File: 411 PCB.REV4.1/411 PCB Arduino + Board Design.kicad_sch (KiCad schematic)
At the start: 37 parts, among them J1 ICSP CONN, J3 Conn_01x04, J4 Conn_01x05_Pin, Q1 Q_NMOS_GDS, SW1 SW_SPST, SW2 SW_MEC_5E, SW3 SW_SPDT, SW4 SW_DPST_x2, U2 ATmega328P-P, Y1 8 MHz

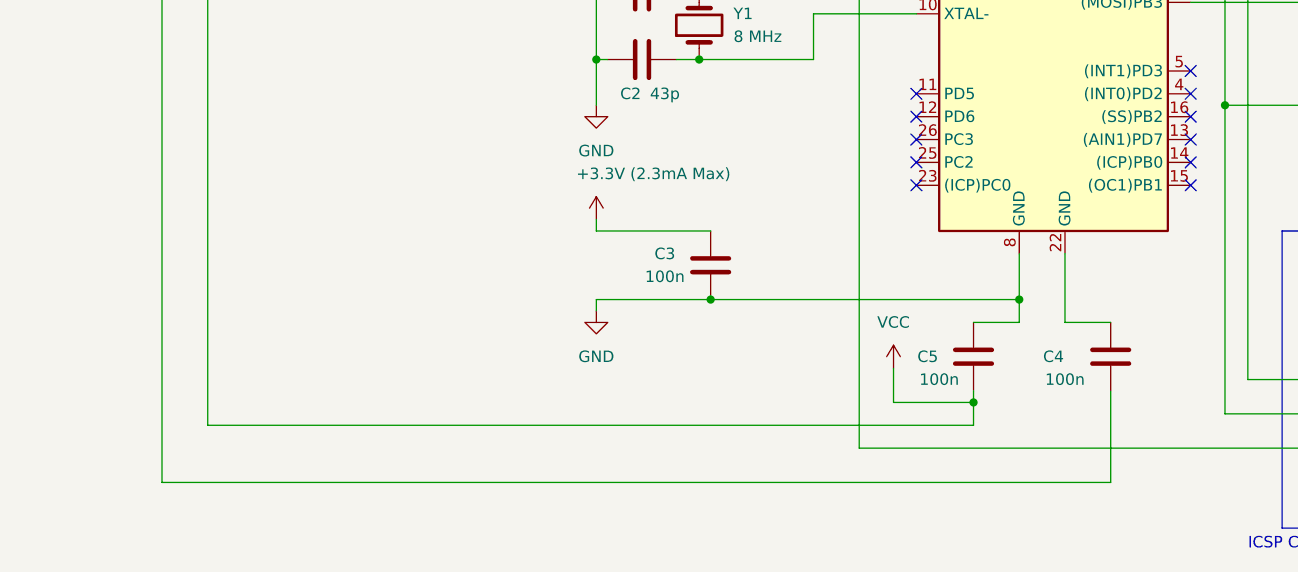
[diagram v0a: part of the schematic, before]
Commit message: removed extra connection to 3.3V for no reason on AVCC line
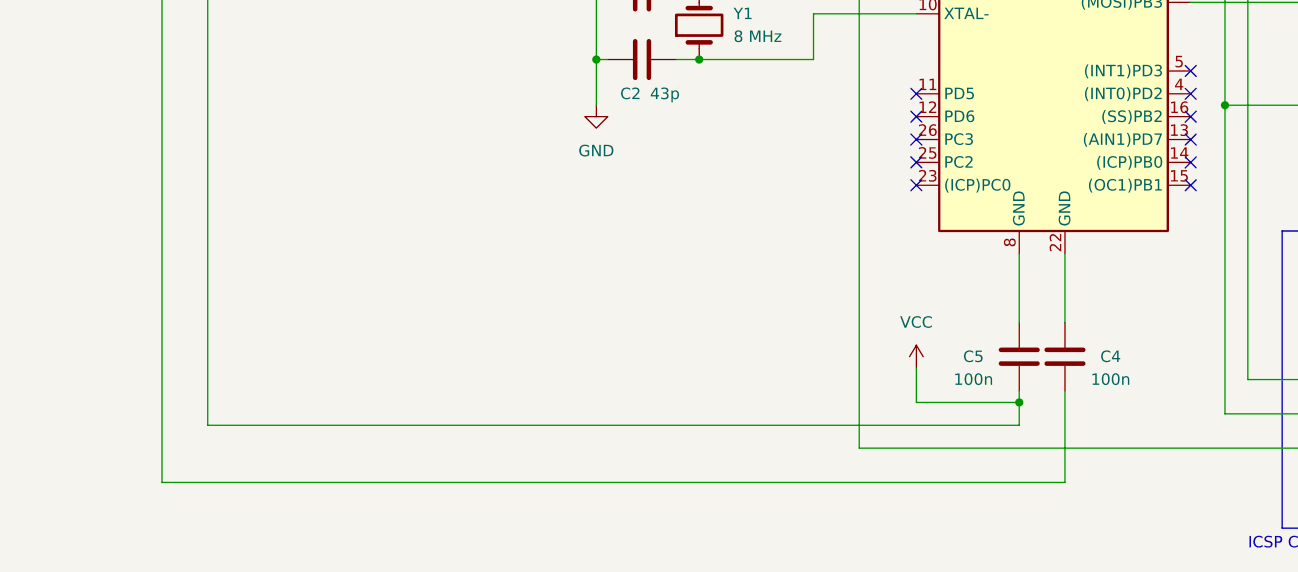
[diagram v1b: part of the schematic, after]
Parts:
- removed C3: 100n, Capacitor_SMD:C_1206_3216Metric_Pad1.33x1.80mm_HandSolder, symbol Device:C
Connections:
- net GND: no longer C5.1, U2.8 (GND)
- new net: C5.1, U2.8 (GND)
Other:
- moved on the sheet: C4, C5
